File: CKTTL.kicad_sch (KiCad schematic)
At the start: 11 parts, among them J4 Conn_01x08_Female, Q1 BC817, U1 LM7805_TO220

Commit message: last TH mounting board
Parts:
- C27: renamed from C3; value 100nF -> 0.1uF; footprint Capacitor_THT:C_Disc_D8.0mm_W5.0mm_P5.00mm -> Capacitor_SMD:C_0603_1608Metric
- C28: renamed from C4; value 100nF -> 0.1uF; footprint Capacitor_THT:C_Disc_D8.0mm_W5.0mm_P5.00mm -> Capacitor_SMD:C_0603_1608Metric
- C29: renamed from C5; value 100nF -> 0.1uF; footprint Capacitor_THT:C_Disc_D8.0mm_W5.0mm_P5.00mm -> Capacitor_SMD:C_0603_1608Metric
- D7, D8: value DIODE -> S1K-13-F; footprint (none) -> Diode_SMD:D_SMA
- R10: renamed from R2; footprint Resistor_THT:R_Axial_DIN0207_L6.3mm_D2.5mm_P5.08mm_Vertical -> Resistor_SMD:R_0603_1608Metric
- R11: renamed from R3; footprint Resistor_THT:R_Axial_DIN0207_L6.3mm_D2.5mm_P5.08mm_Vertical -> Resistor_SMD:R_0603_1608Metric
- R9: renamed from R1; footprint Resistor_THT:R_Axial_DIN0207_L6.3mm_D2.5mm_P5.08mm_Vertical -> Resistor_SMD:R_0603_1608Metric
- renumbered J4 to J15, U1 to U6
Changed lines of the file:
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@@
   (symbol (lib_id "Device:C") (at 171.45 85.09 0) (unit 1)
     (in_bom yes) (on_board yes)
-    (property "Reference" "C5" (id 0) (at 174.371 83.9216 0)
-      (effects (font (size 1.27 1.27)) (justify left))
-    )
-    (property "Value" "100nF" (id 1) (at 174.371 86.233 0)
-      (effects (font (size 1.27 1.27)) (justify left))
-    )
-    (property "Footprint" "Capacitor_THT:C_Disc_D8.0mm_W5.0mm_P5.00mm" (id 2) (at 172.4152 88.9 0)
+    (property "Reference" "C29" (id 0) (at 174.371 83.9216 0)
+      (effects (font (size 1.27 1.27)) (justify left))
+    )
+    (property "Value" "0.1uF" (id 1) (at 174.371 86.233 0)
+      (effects (font (size 1.27 1.27)) (justify left))
+    )
+    (property "Footprint" "Capacitor_SMD:C_0603_1608Metric" (id 2) (at 172.4152 88.9 0)
       (effects (font (size 1.27 1.27)) hide)
     )
@@
   (symbol (lib_id "Device:C") (at 121.92 43.18 0) (unit 1)
     (in_bom yes) (on_board yes)
-    (property "Reference" "C3" (id 0) (at 113.03 42.1386 0)
-      (effects (font (size 1.27 1.27)) (justify left))
-    )
-    (property "Value" "100nF" (id 1) (at 113.03 44.45 0)
-      (effects (font (size 1.27 1.27)) (justify left))
-    )
-    (property "Footprint" "Capacitor_THT:C_Disc_D8.0mm_W5.0mm_P5.00mm" (id 2) (at 122.8852 46.99 0)
+    (property "Reference" "C27" (id 0) (at 113.03 42.1386 0)
+      (effects (font (size 1.27 1.27)) (justify left))
+    )
+    (property "Value" "0.1uF" (id 1) (at 113.03 44.45 0)
+      (effects (font (size 1.27 1.27)) (justify left))
+    )
+    (property "Footprint" "Capacitor_SMD:C_0603_1608Metric" (id 2) (at 122.8852 46.99 0)
       (effects (font (size 1.27 1.27)) hide)
     )
@@
   (symbol (lib_id "power:+5VA") (at 157.48 69.85 0) (unit 1)
     (in_bom yes) (on_board yes) (fields_autoplaced)
-    (property "Reference" "#PWR0103" (id 0) (at 157.48 73.66 0)
+    (property "Reference" "#PWR03" (id 0) (at 157.48 73.66 0)
       (effects (font (size 1.27 1.27)) hide)
     )
@@
       (effects (font (size 1.27 1.27)) (justify left))
     )
-    (property "Value" "DIODE" (id 1) (at 139.192 91.8722 90)
-      (effects (font (size 1.27 1.27)) (justify left))
-    )
-    (property "Footprint" "" (id 2) (at 137.16 90.17 0)
+    (property "Value" "S1K-13-F" (id 1) (at 139.192 91.8722 90)
+      (effects (font (size 1.27 1.27)) (justify left))
+    )
+    (property "Footprint" "Diode_SMD:D_SMA" (id 2) (at 137.16 90.17 0)
       (effects (font (size 1.27 1.27)) hide)
     )
@@
   (symbol (lib_id "Device:R_Small") (at 157.48 74.93 0) (unit 1)
     (in_bom yes) (on_board yes)
-    (property "Reference" "R1" (id 0) (at 158.9786 73.7616 0)
+    (property "Reference" "R9" (id 0) (at 158.9786 73.7616 0)
       (effects (font (size 1.27 1.27)) (justify left))
     )
@@
       (effects (font (size 1.27 1.27)) (justify left))
     )
-    (property "Footprint" "Resistor_THT:R_Axial_DIN0207_L6.3mm_D2.5mm_P5.08mm_Vertical" (id 2) (at 157.48 74.93 0)
+    (property "Footprint" "Resistor_SMD:R_0603_1608Metric" (id 2) (at 157.48 74.93 0)
       (effects (font (size 1.27 1.27)) hide)
     )
@@
       (effects (font (size 1.27 1.27)) hide)
     )
+    (property "Description" "402z" (id 4) (at 157.48 74.93 0)
+      (effects (font (size 1.27 1.27)) hide)
+    )
     (pin "1")
     (pin "2")
@@
   (symbol (lib_id "power:PWR_FLAG") (at 125.73 39.37 0) (unit 1)
     (in_bom yes) (on_board yes)
-    (property "Reference" "#FLG0112" (id 0) (at 125.73 37.465 0)
+    (property "Reference" "#FLG06" (id 0) (at 125.73 37.465 0)
       (effects (font (size 1.27 1.27)) hide)
     )
@@
   (symbol (lib_id "Device:C") (at 147.32 43.18 0) (unit 1)
     (in_bom yes) (on_board yes)
-    (property "Reference" "C4" (id 0) (at 150.241 42.0116 0)
-      (effects (font (size 1.27 1.27)) (justify left))
-    )
-    (property "Value" "100nF" (id 1) (at 150.241 44.323 0)
-      (effects (font (size 1.27 1.27)) (justify left))
-    )
-    (property "Footprint" "Capacitor_THT:C_Disc_D8.0mm_W5.0mm_P5.00mm" (id 2) (at 148.2852 46.99 0)
+    (property "Reference" "C28" (id 0) (at 150.241 42.0116 0)
+      (effects (font (size 1.27 1.27)) (justify left))
+    )
+    (property "Value" "0.1uF" (id 1) (at 150.241 44.323 0)
+      (effects (font (size 1.27 1.27)) (justify left))
+    )
+    (property "Footprint" "Capacitor_SMD:C_0603_1608Metric" (id 2) (at 148.2852 46.99 0)
       (effects (font (size 1.27 1.27)) hide)
     )
@@
   (symbol (lib_id "power:PWR_FLAG") (at 125.73 49.53 0) (unit 1)
     (in_bom yes) (on_board yes)
-    (property "Reference" "#FLG0111" (id 0) (at 125.73 47.625 0)
+    (property "Reference" "#FLG07" (id 0) (at 125.73 47.625 0)
       (effects (font (size 1.27 1.27)) hide)
     )
@@
   (symbol (lib_id "Device:R_Small") (at 146.05 97.79 0) (unit 1)
     (in_bom yes) (on_board yes)
-    (property "Reference" "R3" (id 0) (at 147.5486 96.6216 0)
+    (property "Reference" "R11" (id 0) (at 147.5486 96.6216 0)
       (effects (font (size 1.27 1.27)) (justify left))
     )
@@
       (effects (font (size 1.27 1.27)) (justify left))
     )
-    (property "Footprint" "Resistor_THT:R_Axial_DIN0207_L6.3mm_D2.5mm_P5.08mm_Vertical" (id 2) (at 146.05 97.79 0)
+    (property "Footprint" "Resistor_SMD:R_0603_1608Metric" (id 2) (at 146.05 97.79 0)
       (effects (font (size 1.27 1.27)) hide)
     )
@@
   (symbol (lib_id "Connector:Conn_01x08_Female") (at 92.71 46.99 0) (mirror y) (unit 1)
     (in_bom yes) (on_board yes) (fields_autoplaced)
-    (property "Reference" "J4" (id 0) (at 93.345 37.75 0))
+    (property "Reference" "J15" (id 0) (at 93.345 37.75 0))
     (property "Value" "Conn_01x08_Female" (id 1) (at 93.345 58.7701 0)
       (effects (font (size 1.27 1.27)) hide)
@@
   (symbol (lib_id "Regulator_Linear:LM7805_TO220") (at 135.89 39.37 0) (unit 1)
     (in_bom yes) (on_board yes)
-    (property "Reference" "U1" (id 0) (at 135.89 33.2232 0))
+    (property "Reference" "U6" (id 0) (at 135.89 33.2232 0))
     (property "Value" "LM7805_TO220" (id 1) (at 135.89 35.5346 0))
     (property "Footprint" "Package_TO_SOT_SMD:SOT-223-3_TabPin2" (id 2) (at 135.89 33.655 0)
@@
   (symbol (lib_id "Device:R_Small") (at 121.92 86.36 270) (unit 1)
     (in_bom yes) (on_board yes)
-    (property "Reference" "R2" (id 0) (at 121.92 81.3816 90))
+    (property "Reference" "R10" (id 0) (at 121.92 81.3816 90))
     (property "Value" "4.420k" (id 1) (at 121.92 83.693 90))
-    (property "Footprint" "Resistor_THT:R_Axial_DIN0207_L6.3mm_D2.5mm_P5.08mm_Vertical" (id 2) (at 121.92 86.36 0)
+    (property "Footprint" "Resistor_SMD:R_0603_1608Metric" (id 2) (at 121.92 86.36 0)
       (effects (font (size 1.27 1.27)) hide)
     )
@@
   (symbol (lib_id "power:+5VA") (at 97.79 52.07 270) (unit 1)
     (in_bom yes) (on_board yes) (fields_autoplaced)
-    (property "Reference" "#PWR0102" (id 0) (at 93.98 52.07 0)
+    (property "Reference" "#PWR02" (id 0) (at 93.98 52.07 0)
       (effects (font (size 1.27 1.27)) hide)
     )
@@
   (symbol (lib_id "power:+5VA") (at 156.21 39.37 270) (unit 1)
     (in_bom yes) (on_board yes) (fields_autoplaced)
-    (property "Reference" "#PWR0101" (id 0) (at 152.4 39.37 0)
+    (property "Reference" "#PWR01" (id 0) (at 152.4 39.37 0)
       (effects (font (size 1.27 1.27)) hide)
     )
@@
       (effects (font (size 1.27 1.27)) (justify right))
     )
-    (property "Value" "DIODE" (id 1) (at 130.302 91.8722 90)
+    (property "Value" "S1K-13-F" (id 1) (at 130.302 91.8722 90)
       (effects (font (size 1.27 1.27)) (justify right))
     )
-    (property "Footprint" "" (id 2) (at 128.27 90.17 0)
-      (effects (font (size 1.27 1.27)) hide)
-    )
+    (property "Footprint" "Diode_SMD:D_SMA" (id 2) (at 128.27 90.17 0)
+      (effects (font (size 1.27 1.27)) hide)
+    )

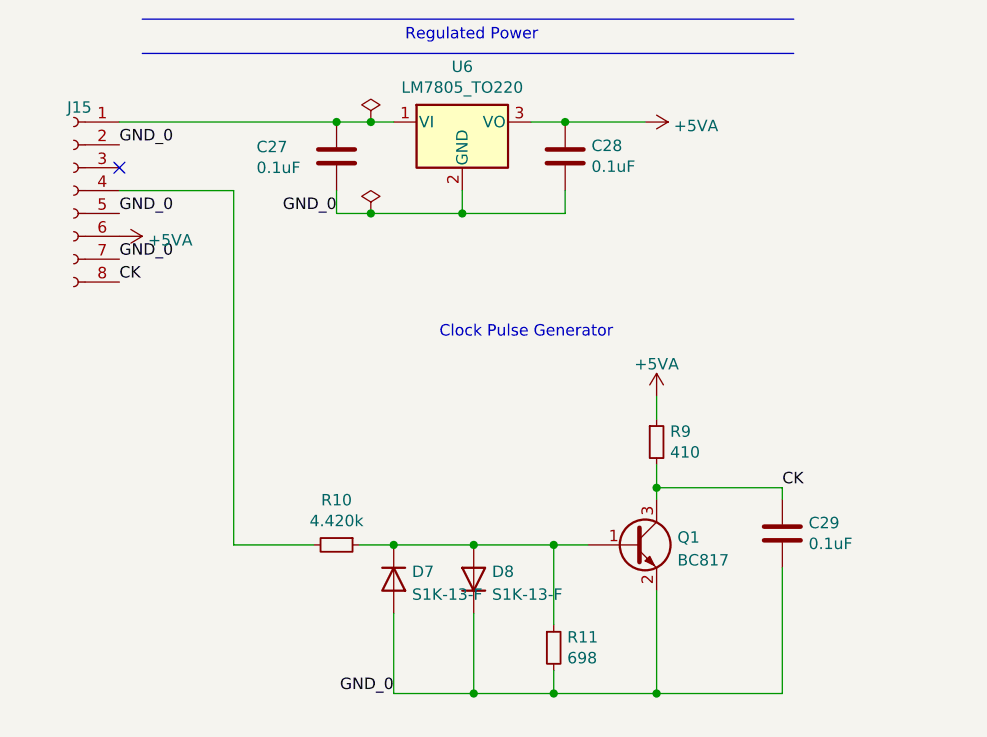
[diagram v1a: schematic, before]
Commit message: all SMD components going into boards
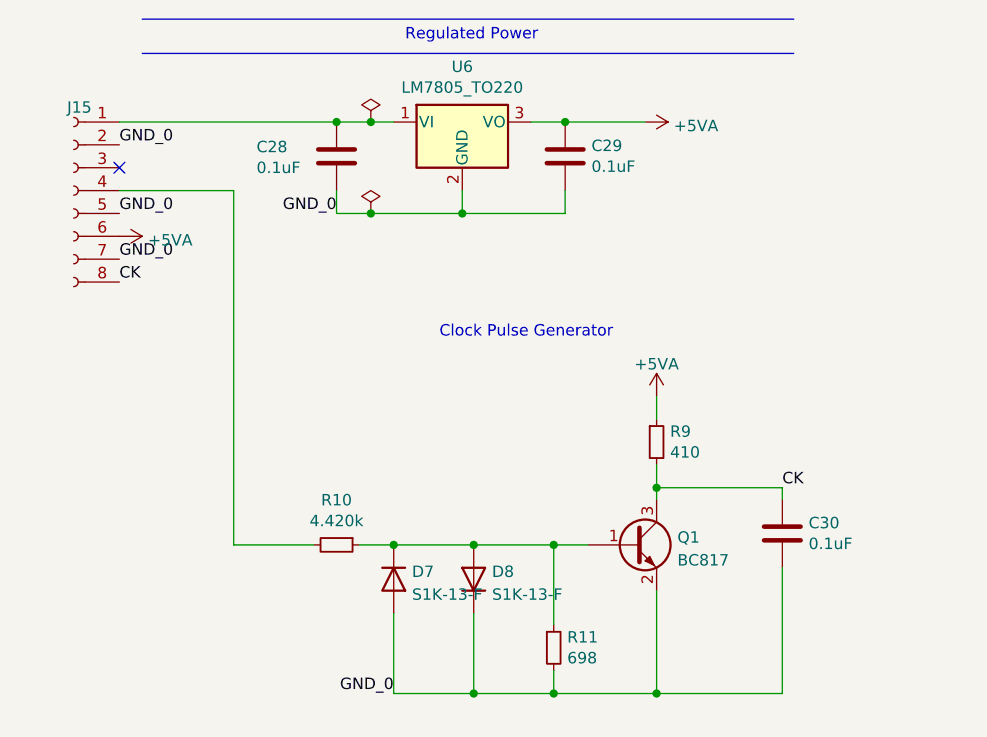
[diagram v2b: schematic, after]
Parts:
- renumbered C27 to C28, C28 to C29, C29 to C30
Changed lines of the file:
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@@
   (symbol (lib_id "Device:C") (at 171.45 85.09 0) (unit 1)
     (in_bom yes) (on_board yes)
-    (property "Reference" "C29" (id 0) (at 174.371 83.9216 0)
+    (property "Reference" "C30" (id 0) (at 174.371 83.9216 0)
       (effects (font (size 1.27 1.27)) (justify left))
     )
@@
   (symbol (lib_id "Device:C") (at 121.92 43.18 0) (unit 1)
     (in_bom yes) (on_board yes)
-    (property "Reference" "C27" (id 0) (at 113.03 42.1386 0)
+    (property "Reference" "C28" (id 0) (at 113.03 42.1386 0)
       (effects (font (size 1.27 1.27)) (justify left))
     )
@@
   (symbol (lib_id "Device:C") (at 147.32 43.18 0) (unit 1)
     (in_bom yes) (on_board yes)
-    (property "Reference" "C28" (id 0) (at 150.241 42.0116 0)
+    (property "Reference" "C29" (id 0) (at 150.241 42.0116 0)
       (effects (font (size 1.27 1.27)) (justify left))
     )

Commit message: new board with SMD
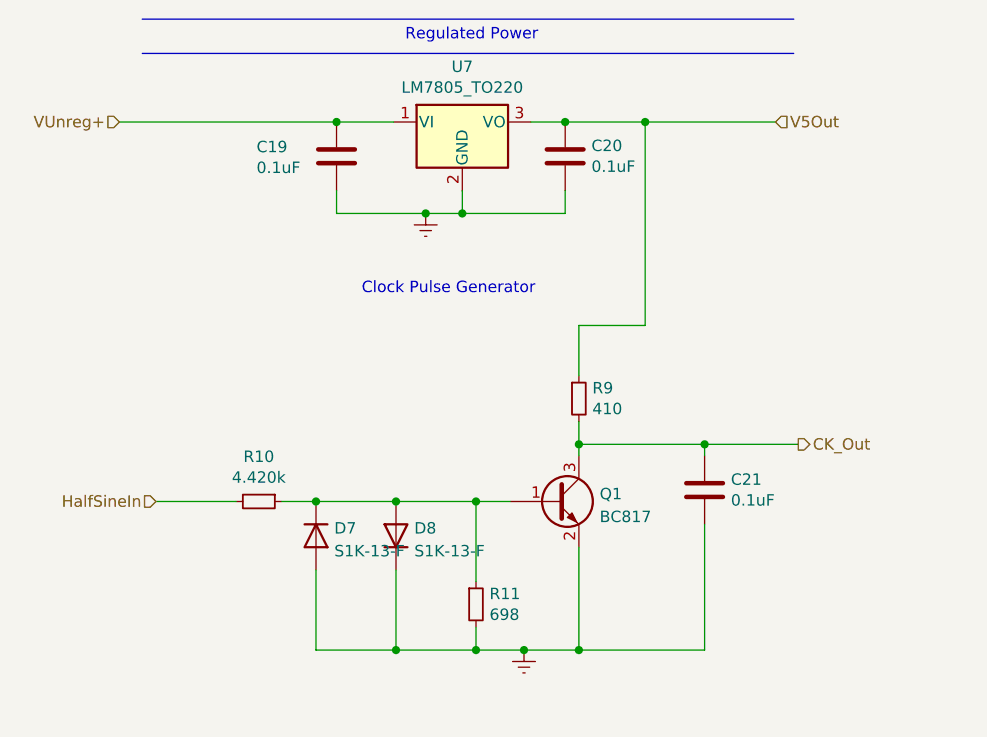
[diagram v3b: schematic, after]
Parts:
- removed J15: Conn_01x08_Female, Connector_PinHeader_2.54mm:PinHeader_1x08_P2.54mm_Vertical, symbol Connector:Conn_01x08_Female
- renumbered C28 to C19, C29 to C20, C30 to C21, U6 to U7
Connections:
- net VUnreg+: now reaches C19.1, U7.1 (VI)
- net HalfSineIn: now reaches R10.2
- net +5VA renamed V5Out
- net CK renamed CK_Out
- net GND_0 renamed GNDREF
- no-connect marks 1 -> 0
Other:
- moved on the sheet: C21, D7, D8, Q1, R10, R11, R9

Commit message: Updated improved board for all SMD
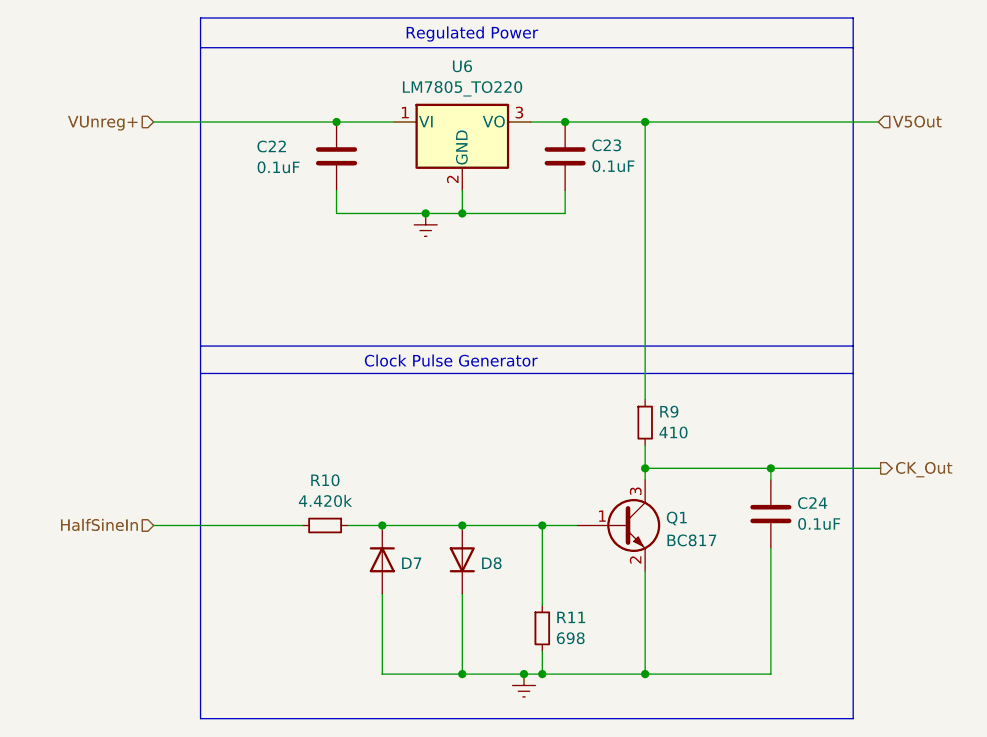
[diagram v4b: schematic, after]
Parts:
- renumbered C19 to C22, C20 to C23, C21 to C24, U7 to U6
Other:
- moved on the sheet: C24, D7, D8, Q1, R10, R11, R9

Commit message: added new op amps and used automated traces due to complexity
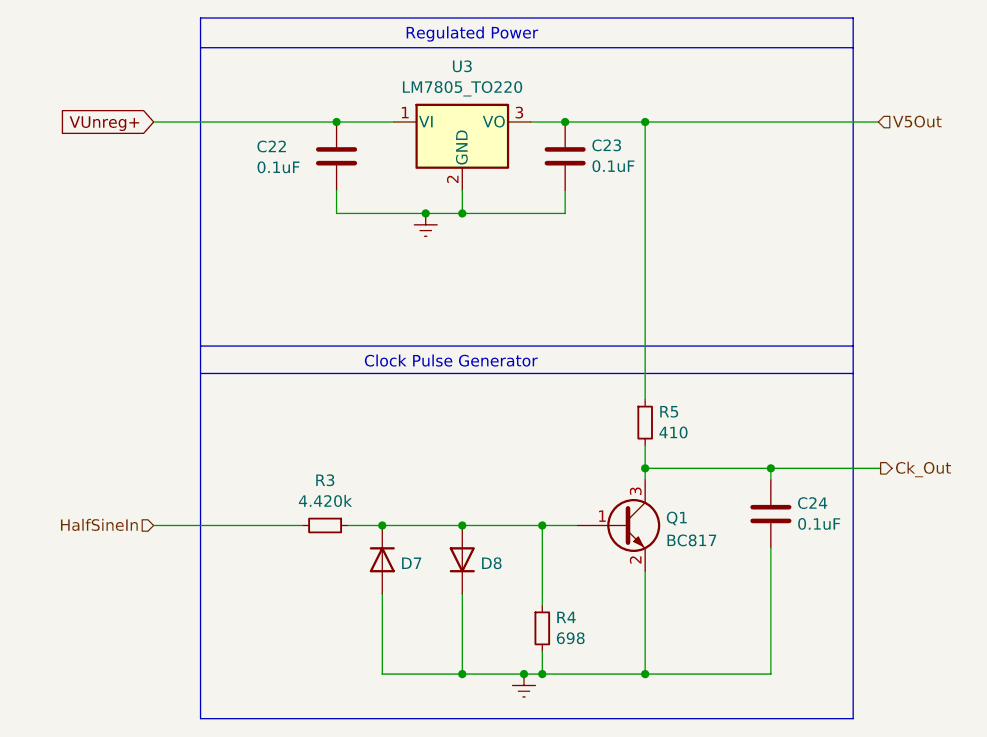
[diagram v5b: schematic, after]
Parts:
- renumbered R10 to R3, R11 to R4, R9 to R5, U6 to U3
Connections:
- net CK_Out renamed Ck_Out
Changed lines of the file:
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@@
     (effects (font (size 1.27 1.27)) (justify left bottom))
   )
-  (hierarchical_label "CK_Out" (shape output) (at 182.372 77.851 0)
+  (global_label "VUnreg+" (shape input) (at 101.6 39.37 180) (fields_autoplaced)
+    (effects (font (size 1.27 1.27)) (justify right))
+    (property "Intersheet References" "${INTERSHEET_REFS}" (id 0) (at 91.1115 39.2906 0)
+      (effects (font (size 1.27 1.27)) (justify right))
+    )
+  )
+  (hierarchical_label "Ck_Out" (shape output) (at 182.372 77.851 0)
     (effects (font (size 1.27 1.27)) (justify left))
   )
@@
   )
   (hierarchical_label "HalfSineIn" (shape input) (at 101.6 84.201 180)
-    (effects (font (size 1.27 1.27)) (justify right))
-  )
-  (hierarchical_label "VUnreg+" (shape input) (at 101.6 39.37 180)
     (effects (font (size 1.27 1.27)) (justify right))
   )
@@
   (symbol (lib_id "Device:R_Small") (at 156.21 72.771 0) (unit 1)
     (in_bom yes) (on_board yes)
-    (property "Reference" "R9" (id 0) (at 157.7086 71.6026 0)
+    (property "Reference" "R5" (id 0) (at 157.7086 71.6026 0)
       (effects (font (size 1.27 1.27)) (justify left))
     )
@@
   (symbol (lib_id "Device:R_Small") (at 144.78 95.631 0) (unit 1)
     (in_bom yes) (on_board yes)
-    (property "Reference" "R11" (id 0) (at 146.2786 94.4626 0)
+    (property "Reference" "R4" (id 0) (at 146.2786 94.4626 0)
       (effects (font (size 1.27 1.27)) (justify left))
     )
@@
   (symbol (lib_id "Regulator_Linear:LM7805_TO220") (at 135.89 39.37 0) (unit 1)
     (in_bom yes) (on_board yes)
-    (property "Reference" "U6" (id 0) (at 135.89 33.2232 0))
+    (property "Reference" "U3" (id 0) (at 135.89 33.2232 0))
     (property "Value" "LM7805_TO220" (id 1) (at 135.89 35.5346 0))
     (property "Footprint" "Package_TO_SOT_SMD:SOT-223-3_TabPin2" (id 2) (at 135.89 33.655 0)
@@
   (symbol (lib_id "Device:R_Small") (at 120.65 84.201 270) (unit 1)
     (in_bom yes) (on_board yes)
-    (property "Reference" "R10" (id 0) (at 120.65 79.2226 90))
+    (property "Reference" "R3" (id 0) (at 120.65 79.2226 90))
     (property "Value" "4.420k" (id 1) (at 120.65 81.534 90))
     (property "Footprint" "Resistor_SMD:R_0603_1608Metric" (id 2) (at 120.65 84.201 0)
